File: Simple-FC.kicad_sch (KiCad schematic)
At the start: 49 parts, among them J1 USB_C_Receptacle_USB2.0_14P, J2 Micro_SD_Card, SW1 SW_Push, U1 RP2350A, U2 MMC5983MA, U3 LSM6DSM, U4 BMP384, U5 TPS631000, U6 W25Q128JVS, Y1 ABM8-272-T3

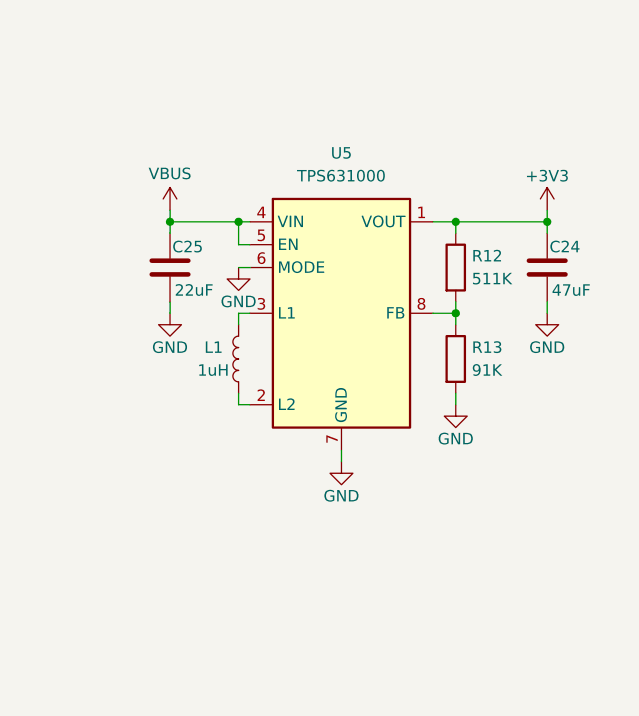
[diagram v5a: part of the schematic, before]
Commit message: added gpio to regulator mode
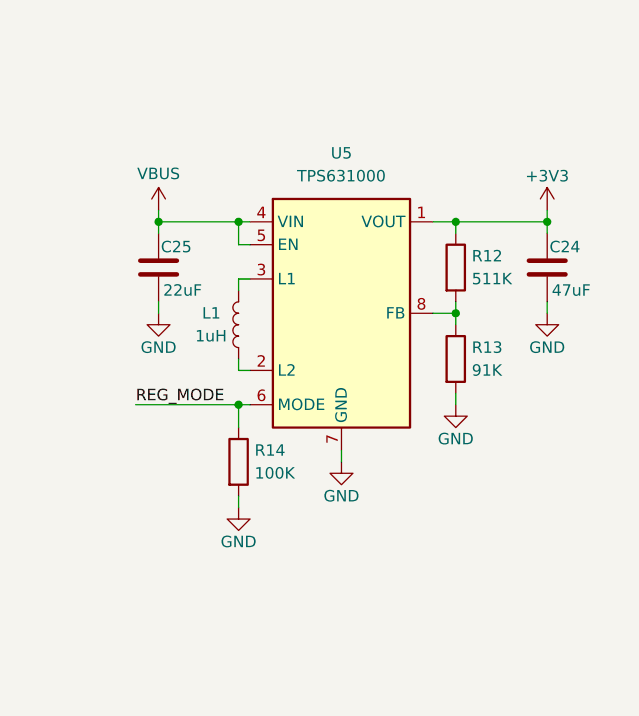
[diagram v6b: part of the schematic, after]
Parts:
- added R14: 100K, Resistor_SMD:R_0402_1005Metric, symbol Device:R
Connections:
- net GND: now also R14.2; no longer U5.6 (MODE)
- new net REG_MODE: R14.1, U5.6 (MODE)
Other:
- moved on the sheet: C25

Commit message: routing mcu reg
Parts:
- added C26, C27, C28: 4.7uF, Capacitor_SMD:C_0402_1005Metric, symbol Device:C
- added L2: L, Package_TO_SOT_SMD:SOT-583-8, symbol Device:L
- added R15: 33, Resistor_SMD:R_0402_1005Metric, symbol Device:R
- C10, C4: value 1uF -> 4.7uF
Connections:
- net +1V1: now also U1.23 (DVDD), U1.39 (DVDD), U1.50 (VREG_FB), U1.6 (DVDD), C27.1, L2.2
- net +3V3: now also R15.1
- net GND: now also U1.47 (VREG_PGND), U1.61 (GND), C26.2, C27.2
- net at U1.46 (VREG_AVDD): now also C26.1, R15.2
- net at U1.48 (VREG_LX): now also L2.1
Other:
- moved on the sheet: C10, C11, C12, C13, C14, C15, C16, C4, C6, C7, C8, C9

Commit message: finished mcu power circuit
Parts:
- removed C27: 4.7uF, Capacitor_SMD:C_0402_1005Metric, symbol Device:C
- added C29: 4.7uF, Capacitor_SMD:C_0402_1005Metric, symbol Device:C
- L2: value L -> 3.3uH
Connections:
- net +1V1: now also C28.1, L2.1; no longer L2.2
- net +3V3: now also U1.1 (IOVDD), U1.11 (IOVDD), U1.20 (IOVDD), U1.30 (IOVDD), U1.38 (IOVDD), U1.44 (ADC_AVDD), U1.45 (IOVDD), U1.49 (VREG_VIN), U1.53 (USB_OTP_VDD), U1.54 (QSPI_IOVDD), C29.1
- net GND: now also C28.2, C29.2
- net at U1.48 (VREG_LX): now also L2.2; no longer L2.1
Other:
- moved on the sheet: C10, C11, C12, C13, C14, C15, C16, C4, C6, C7, C8, C9
